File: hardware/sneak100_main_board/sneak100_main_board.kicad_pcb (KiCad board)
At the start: 2 copper layers, 50 x 72 mm, 111 parts, among them J1 USB_OTG, J10 Conn_01x02, J11 Conn_01x03, J12 Conn_01x03, J13 Conn_01x03, J14 Conn_01x03, J2 Conn_01x06, J3 Conn_01x04, J4 Conn_01x02, J5 Conn_01x06, J6 Conn_01x06, J7 Conn_01x06, J8 Conn_01x06, J9 Conn_01x03, Q1 Q_PMOS_DGS, Q2 Q_PMOS_DGS, Q3 SFH-313FA, Q4 SFH-313FA, Q5 SFH-313FA, Q6 SFH-313FA, Q7 SFH-313FA, Q8 SFH-313FA, SW1 SW_Push, SW2 SW_Push, SW3 SW_Push_SPDT, U1 TSOP4838, U2 DRV8835, U3 DRV8835, U4 DRV8835, U5 DRV8835, U6 LM1117-3.3, U7 CD4051B, U8 CD4051B, U9 STM32F405RGTx, Y1 8MHz

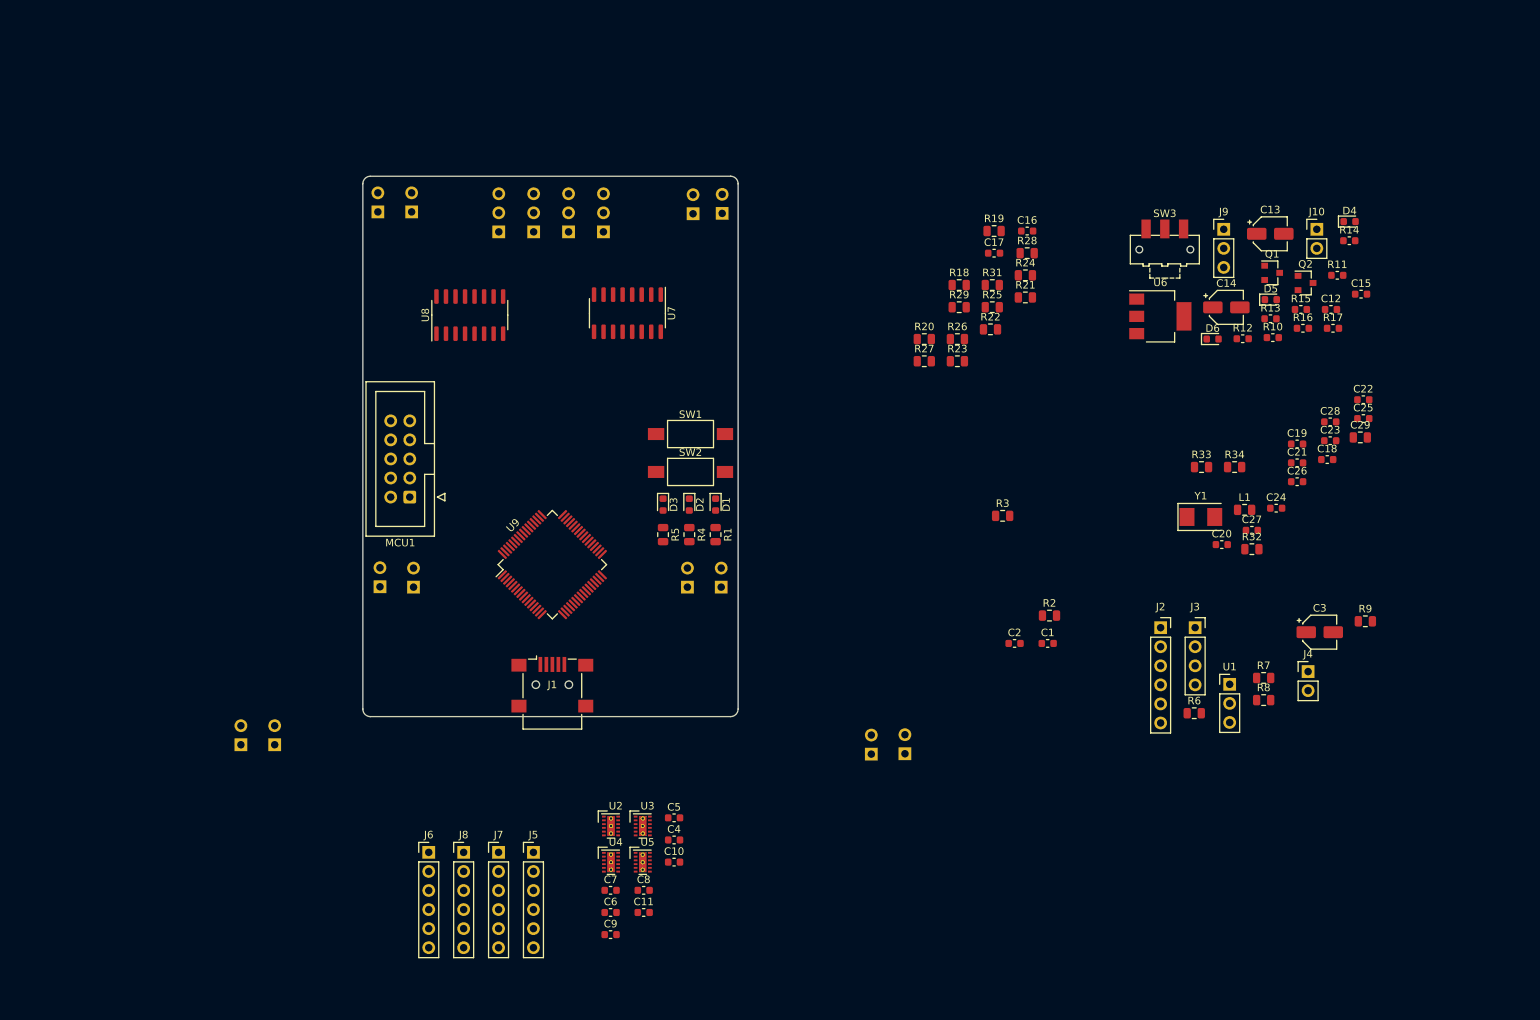
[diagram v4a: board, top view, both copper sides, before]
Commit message: USB FDU mode
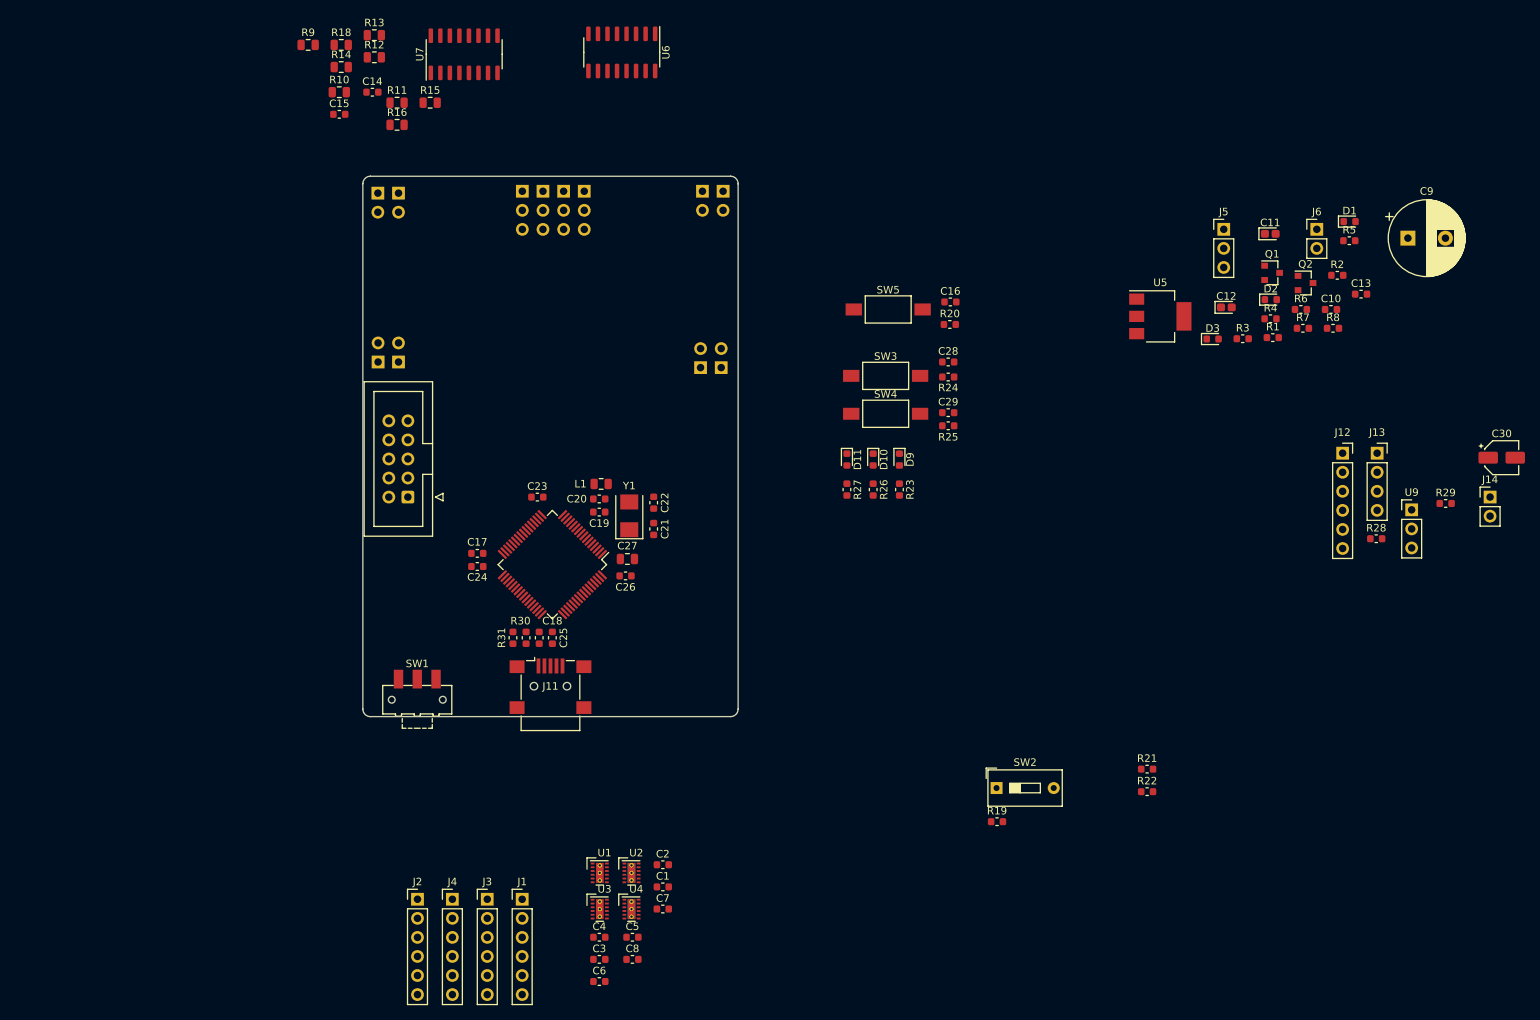
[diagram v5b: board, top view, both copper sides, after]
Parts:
- removed the D11 at (106.5, 117.2)
- removed D12: SFH4550, Connector_PinHeader_2.54mm:PinHeader_1x02_P2.54mm_Vertical
- removed Q7, Q8: SFH-313FA, Connector_PinHeader_2.54mm:PinHeader_1x02_P2.54mm_Vertical
- removed the R22 at (206.4, 61.9)
- removed the R23 at (202.0, 66.2)
- removed the R28 at (211.3, 51.8)
- removed the R29 at (202.2, 59.0)
- added C9: 780uF, Capacitor_THT:CP_Radial_D10.0mm_P5.00mm, F.Cu at (262.0, 49.8)
- added R19: 4k7, Resistor_SMD:R_0603_1608Metric, F.Cu at (207.2, 127.5)
- added SW2: SW_SPST, Button_Switch_THT:SW_DIP_SPSTx01_Slide_9.78x4.72mm_W7.62mm_P2.54mm, F.Cu at (207.2, 123.0)
- added SW5: SW_Push, Button_Switch_SMD:SW_SPST_FSMSM, F.Cu at (192.8, 59.2)
- C11: renamed from C13; footprint Capacitor_SMD:CP_Elec_4x3 -> Capacitor_Tantalum_SMD:CP_EIA-1608-10_AVX-L
- C12: renamed from C14; footprint Capacitor_SMD:CP_Elec_4x3 -> Capacitor_Tantalum_SMD:CP_EIA-1608-10_AVX-L
- R20: renamed from R32; value 10k -> 4k7; footprint Resistor_SMD:R_0805_2012Metric -> Resistor_SMD:R_0603_1608Metric
- R21: renamed from R33; footprint Resistor_SMD:R_0805_2012Metric -> Resistor_SMD:R_0603_1608Metric
- R22: renamed from R34; footprint Resistor_SMD:R_0805_2012Metric -> Resistor_SMD:R_0603_1608Metric
- R23: renamed from R1; footprint Resistor_SMD:R_0805_2012Metric -> Resistor_SMD:R_0603_1608Metric
- R24: renamed from R2; footprint Resistor_SMD:R_0805_2012Metric -> Resistor_SMD:R_0603_1608Metric
- R25: renamed from R3; footprint Resistor_SMD:R_0805_2012Metric -> Resistor_SMD:R_0603_1608Metric
- R26: renamed from R4; footprint Resistor_SMD:R_0805_2012Metric -> Resistor_SMD:R_0603_1608Metric
- R27: renamed from R5; footprint Resistor_SMD:R_0805_2012Metric -> Resistor_SMD:R_0603_1608Metric
- R28: renamed from R6; footprint Resistor_SMD:R_0805_2012Metric -> Resistor_SMD:R_0603_1608Metric
- R29: renamed from R7; footprint Resistor_SMD:R_0805_2012Metric -> Resistor_SMD:R_0603_1608Metric
- R30: renamed from R8; footprint Resistor_SMD:R_0805_2012Metric -> Resistor_SMD:R_0603_1608Metric
- R31: renamed from R9; footprint Resistor_SMD:R_0805_2012Metric -> Resistor_SMD:R_0603_1608Metric
- moved SW1 116.3 mm to (130.0, 111.2)
- moved R31 113.6 mm to (142.8, 103.0), turned to 90 degrees
- moved C23 110.6 mm to (146.0, 84.2)
- moved C17 110.2 mm to (138.0, 91.8), turned to 180 degrees
- moved C24 109.8 mm to (138.0, 93.5), turned to 180 degrees
- moved C20 102.7 mm to (154.2, 84.5)
- moved C27 99.0 mm to (158.0, 92.5)
- moved R30 98.6 mm to (144.5, 103.0), turned to 270 degrees
- moved C26 96.1 mm to (157.8, 94.8)
- moved C25 94.3 mm to (148.0, 103.0), turned to 270 degrees
- moved C19 93.2 mm to (154.2, 86.2)
- moved R9 92.5 mm to (115.5, 24.0)
- moved R12 92.5 mm to (124.3, 25.6)
- moved R13 92.5 mm to (124.3, 22.7)
- moved R14 92.5 mm to (119.9, 26.9)
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- renumbered C4 to C1, C12 to C10, C15 to C13, C16 to C14, C17 to C15, C18 to C16, C19 to C17, C20 to C18, C21 to C19, C5 to C2, C22 to C20, C23 to C21, C24 to C22, C25 to C23, C26 to C24, C27 to C25, C28 to C26, C29 to C27, C1 to C28, C2 to C29, C6 to C3, C3 to C30, C7 to C4, C8 to C5, C9 to C6, C10 to C7, C11 to C8, D4 to D1, D2 to D10, D3 to D11, D5 to D2, D6 to D3, D7 to D4, D8 to D5, D9 to D6, D10 to D7, D1 to D9, J5 to J1, J14 to J10, J1 to J11, J2 to J12, J3 to J13, J4 to J14, J6 to J2, J7 to J3, J8 to J4, J9 to J5, J10 to J6, J11 to J7, J12 to J8, J13 to J9, R10 to R1, R19 to R10, R20 to R11, R21 to R12, R24 to R13, R25 to R14, R26 to R15, R27 to R16, R31 to R18, R11 to R2, R12 to R3, R13 to R4, R14 to R5, R15 to R6, R16 to R7, R17 to R8, R18 to R9, SW3 to SW1, SW1 to SW3, SW2 to SW4, U2 to U1, U3 to U2, U4 to U3, U5 to U4, U6 to U5, U7 to U6, U8 to U7, U9 to U8, U1 to U9
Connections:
- C16 pad 1: /interface/BUTTON2 -> Net-(C16-Pad1)
- J10 pad 1: /controller/LINE_RR -> GND
- J10 pad 3: GND -> /controller/LINE_RR
- J7 pad 1: /controller/LINE_LL -> GND
- J7 pad 3: GND -> /controller/LINE_LL
- J8 pad 1: /controller/LINE_LM -> GND
- J8 pad 3: GND -> /controller/LINE_LM
- J9 pad 1: /controller/LINE_RM -> GND
- J9 pad 3: GND -> /controller/LINE_RM
- MCU1 pad 1: /interface/BUTTON2 -> (no net)
- Q3 pad 1: /proximitySensors/RX_IN1 -> GND
- Q3 pad 2: GND -> /proximitySensors/RX_IN1
- Q4 pad 1: /proximitySensors/RX_IN2 -> GND
- Q4 pad 2: GND -> /proximitySensors/RX_IN2
- Q5 pad 1: /proximitySensors/RX_IN3 -> GND
- Q5 pad 2: GND -> /proximitySensors/RX_IN3
- Q6 pad 1: /proximitySensors/RX_IN4 -> GND
- Q6 pad 2: GND -> /proximitySensors/RX_IN4
- R20 pad 2: /interface/BUTTON2 -> Net-(C16-Pad1)
- U6 pad 1: /proximitySensors/TX_OUT5 -> (no net)
- U6 pad 5: /proximitySensors/TX_OUT6 -> (no net)
- U7 pad 1: /proximitySensors/RX_IN5 -> (no net)
- U7 pad 5: /proximitySensors/RX_IN6 -> (no net)
- U8 pad 28: (no net) -> GND
- U8 pad 53: /interface/BUTTON1 -> /interface/BUTTON2
- U8 pad 7: /interface/BUTTON2 -> Net-(C16-Pad1)

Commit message: Layout progress
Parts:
- removed the C16 at (201.0, 58.2)
- removed C29: 100nF, Capacitor_SMD:C_0603_1608Metric
- removed the J13 at (257.9, 78.4)
- removed the R25 at (200.8, 74.8)
- removed the SW2 at (207.2, 123.0)
- removed SW4, SW5: SW_Push, Button_Switch_SMD:SW_SPST_FSMSM
- added J14: Conn_02x02_Odd_Even, Connector_PinHeader_2.54mm:PinHeader_2x02_P2.54mm_Vertical, F.Cu at (126.5, 92.7)
- C17: renamed from C30; footprint Capacitor_SMD:CP_Elec_4x3 -> Capacitor_THT:CP_Radial_D5.0mm_P2.00mm
- J1, J2, J3, J4: footprint Connector_PinHeader_2.54mm:PinHeader_1x06_P2.54mm_Vertical -> Connector_JST:JST_PH_S6B-PH-K_1x06_P2.00mm_Horizontal; moved to B.Cu
- moved SW1 116.6 mm to (227.0, 46.5)
- moved C3 74.6 mm to (155.8, 71.2)
- moved C4 69.2 mm to (155.8, 73.8)
- moved C1 68.3 mm to (140.8, 71.5)
- moved U1 64.1 mm to (137.2, 72.5)
- moved C6 64.0 mm to (140.8, 86.2)
- moved J2 63.9 mm to (148.8, 76.8)
- moved C2 62.9 mm to (140.8, 74.2)
- moved U2 62.4 mm to (152.2, 72.2)
- moved J1 62.0 mm to (133.5, 76.8)
- moved J4 62.0 mm to (158.8, 80.8), turned to 180 degrees
- moved C5 61.9 mm to (140.5, 83.8)
- moved C8 59.9 mm to (156.8, 86.0)
- moved J3 57.2 mm to (143.5, 80.8), turned to 180 degrees
- moved U3 56.9 mm to (137.0, 85.0)
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- renumbered C28 to C16, C17 to C18, C18 to C19, C19 to C20, C20 to C21, C21 to C22, C22 to C23, C23 to C24, C24 to C25, C25 to C26, C26 to C27, C27 to C28, J14 to J13, R23 to R19, R24 to R20, R26 to R21, R27 to R22, R28 to R23, R29 to R24, R30 to R25, R31 to R26, R19 to R27, R20 to R28, R21 to R29, R22 to R30, SW3 to SW2, U9 to U8, U8 to U9
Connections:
- C16 pad 1: /interface/BUTTON1 -> /interface/BUTTON
- MCU1 pad 1: (no net) -> /controller/RST
- MCU1 pad 7: +3V3 -> ST-LINK_3.3V
- MCU1 pad 8: +3V3 -> ST-LINK_3.3V
- R20 pad 2: /interface/BUTTON1 -> /interface/BUTTON
- R27 pad 2: Net-(R19-Pad2) -> /controller/BOOT0
- R28 pad 2: Net-(C16-Pad1) -> /controller/RST
- SW2 pad 2: /interface/BUTTON1 -> /interface/BUTTON
- U9 pad 2: /controller/MODULE_START -> (no net)
- U9 pad 3: /controller/MODULE_KILL -> (no net)
- U9 pad 53: /interface/BUTTON2 -> /interface/BUTTON
- U9 pad 60: GND -> /controller/BOOT0
- U9 pad 7: Net-(C16-Pad1) -> /controller/RST

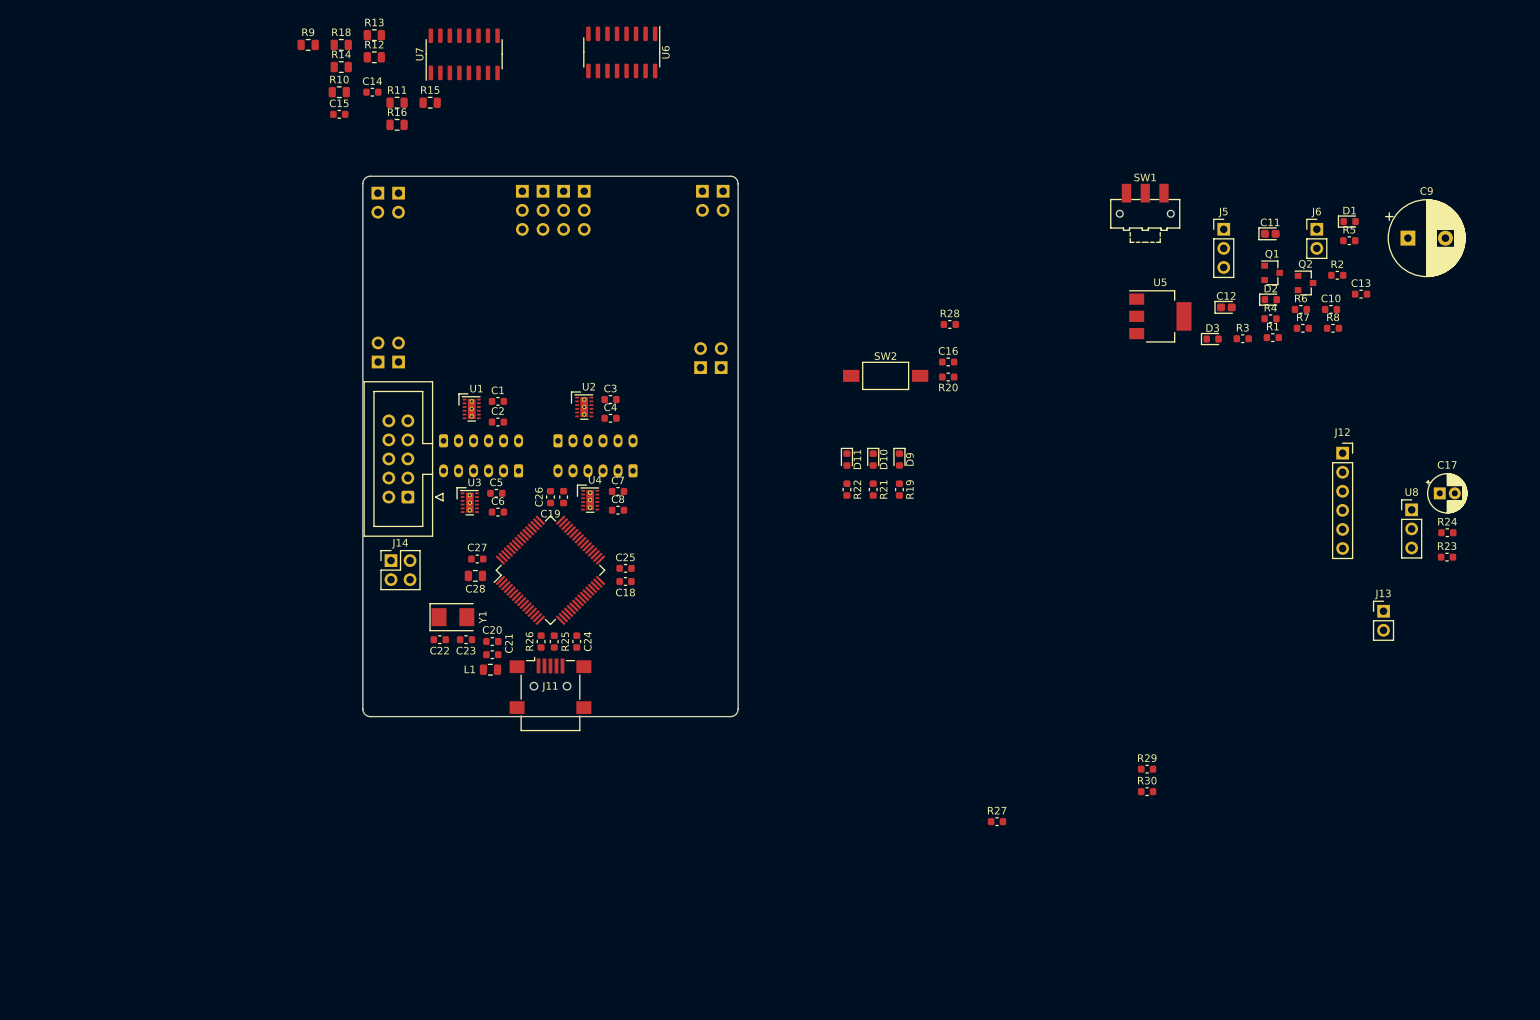
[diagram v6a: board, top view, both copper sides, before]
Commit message: Add OLED display
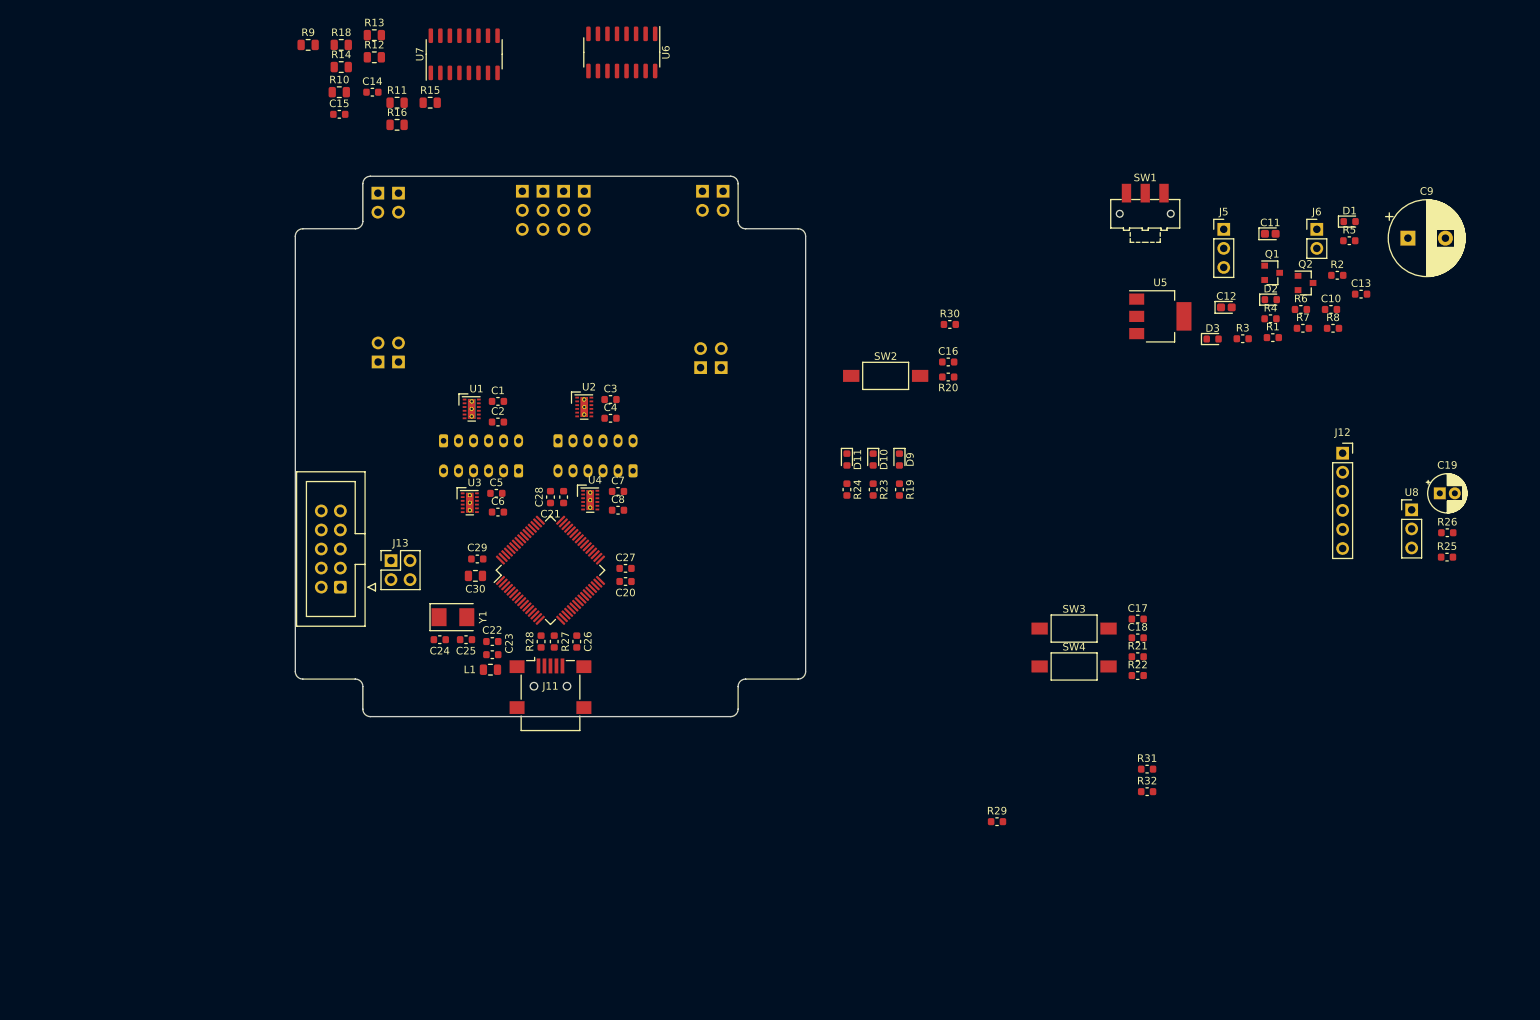
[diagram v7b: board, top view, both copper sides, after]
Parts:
- removed the J13 at (258.8, 99.5)
- added C17: 100nF, Capacitor_SMD:C_0603_1608Metric, F.Cu at (226.0, 100.5)
- added C18: 100nF, Capacitor_SMD:C_0603_1608Metric, F.Cu at (226.0, 103.0)
- added R21: 4k7, Resistor_SMD:R_0603_1608Metric, F.Cu at (226.0, 105.5)
- added R22: 4k7, Resistor_SMD:R_0603_1608Metric, F.Cu at (226.0, 108.0)
- added SW3: SW_Push, Button_Switch_SMD:SW_SPST_FSMSM, F.Cu at (217.5, 101.8)
- added SW4: SW_Push, Button_Switch_SMD:SW_SPST_FSMSM, F.Cu at (217.5, 106.8)
- moved MCU1 15.0 mm to (119.8, 96.2)
- renumbered C17 to C19, C18 to C20, C19 to C21, C20 to C22, C21 to C23, C22 to C24, C23 to C25, C24 to C26, C25 to C27, C26 to C28, C27 to C29, C28 to C30, J14 to J13, R21 to R23, R22 to R24, R23 to R25, R24 to R26, R25 to R27, R26 to R28, R27 to R29, R28 to R30, R29 to R31, R30 to R32
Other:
- board size 50 x 72 mm -> 68 x 72 mm
